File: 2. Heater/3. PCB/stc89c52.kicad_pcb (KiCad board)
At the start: 2 copper layers, 85 x 100 mm, 38 parts, among them IC1 STC89C52rc, J1 USB-Type-C, K1 relay, Q1 S8050, SW1 3x4, SW2 up, SW3 down, SW4 switch, SW5 ctrl, U1 ADC0832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

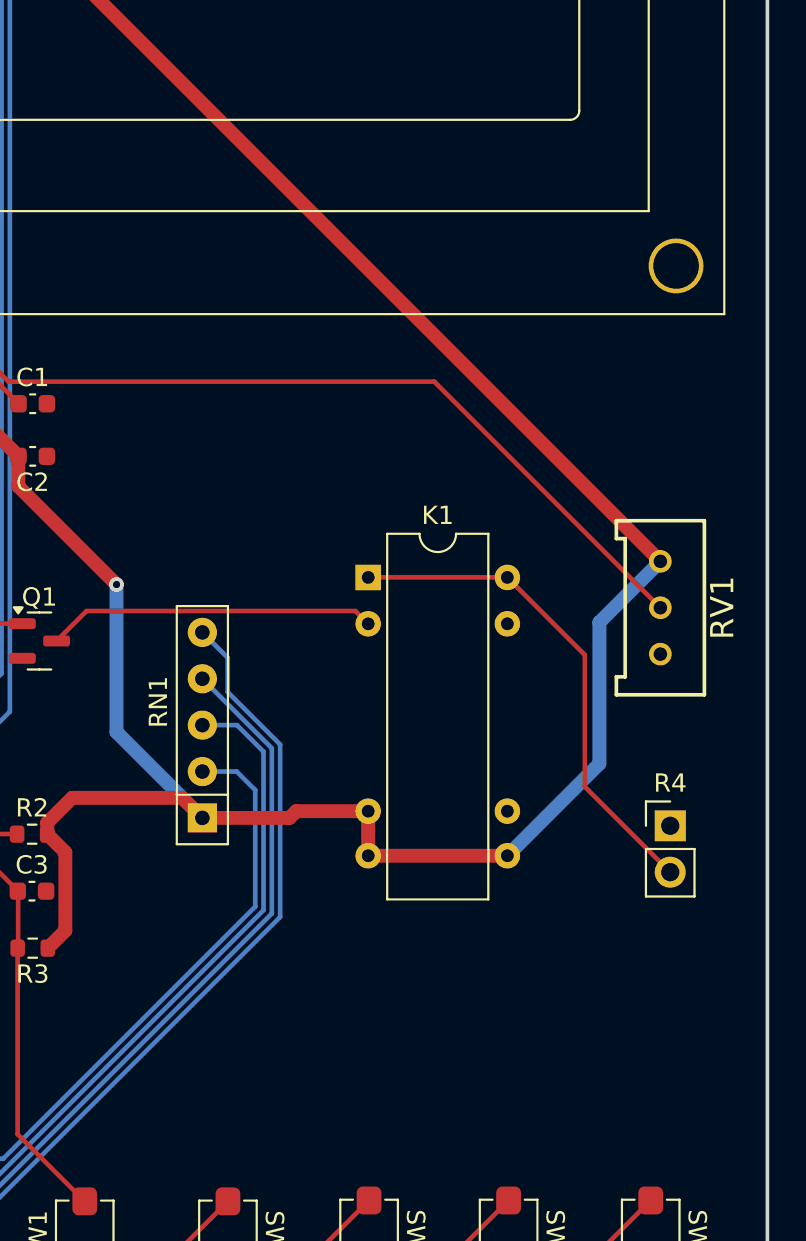
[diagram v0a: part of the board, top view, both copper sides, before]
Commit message: add 24v conn
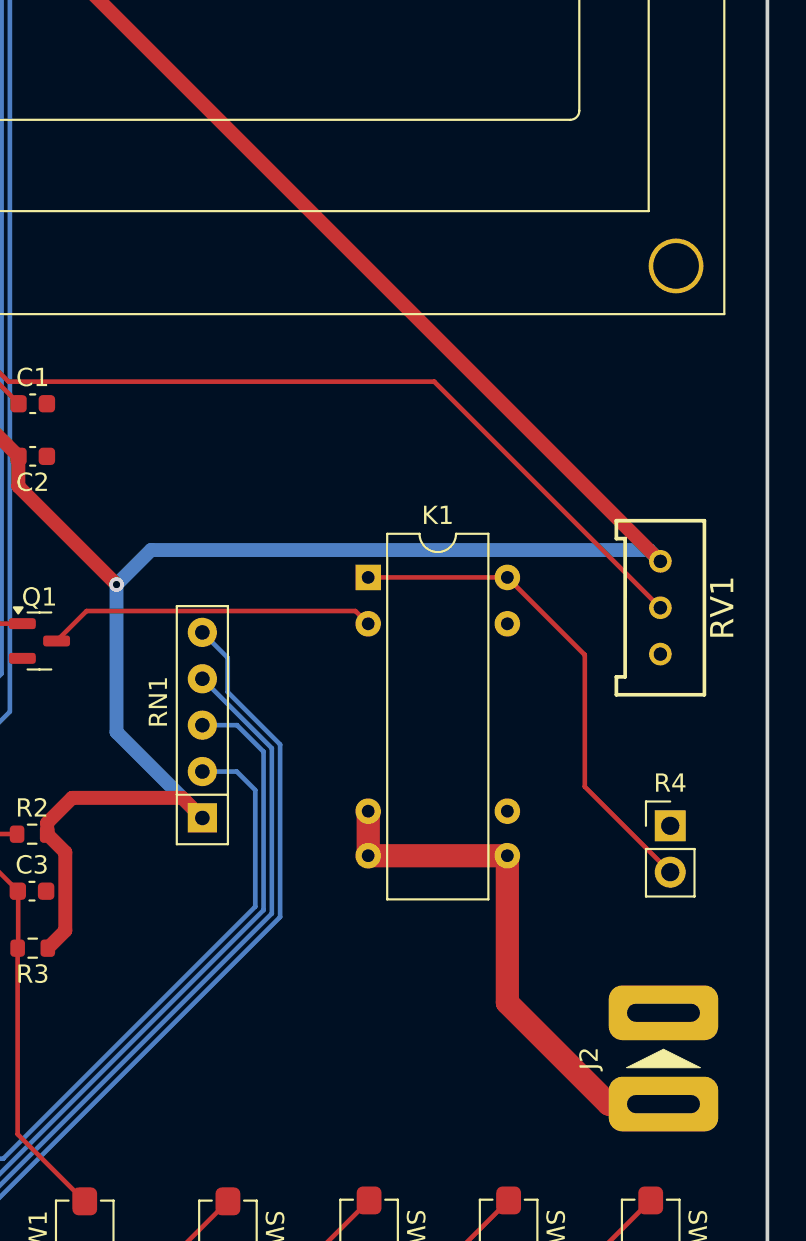
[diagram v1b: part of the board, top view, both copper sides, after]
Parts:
- added J2: Conn_01x02, ErBW_s:VCC_CONN, F.Cu at (186.8, 125.6)
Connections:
- K1 pad 6: VCC -> 24V
- K1 pad 7: VCC -> 24V
- K1 pad 8: VCC -> 24V
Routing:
- net 24V: track 0.00 -> 29.0 mm
- net VCC: track 276.5 -> 268.4 mm
